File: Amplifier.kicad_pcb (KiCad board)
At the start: 2 copper layers, 140 x 54 mm, 26 parts, among them J2 Input, J3 Conn_01x04, J4 output, T1 Transformer_SP_1S, U1 6N2P, U2 6P14P

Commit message: New amplifier PCB
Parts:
- removed C1: 10uF, spdf1626_lib:C_THT_D5.0mm_P2.54mm
- removed C12, C13: 10uF, spdf1626_lib:C_THT_D10.0mm_P5.00mm
- removed J4: output, spdf1626_lib:PinHeader_1x02_P2.54mm
- removed R12: 680R, spdf1626_lib:R_THT_025W
- added C10: 10uF, spdf1626_lib:C_THT_D5.0mm_P2.5mm, F.Cu at (63.8, 55.0)
- added C4: 10uF, spdf1626_lib:C_THT_D10.0mm_P5.00mm, F.Cu at (95.9, 47.2)
- added C5: 100n, spdf1626_lib:C_THT_K73-17_P9.00mm, F.Cu at (107.1, 85.5)
- added J1: Input, spdf1626_lib:PinHeader_1x02_P2.54mm, F.Cu at (114.1, 50.7)
- added R10: 220R*, spdf1626_lib:R_THT_1W, F.Cu at (72.6, 62.0)
- C2: value 10uF -> 100n; footprint spdf1626_lib:C_THT_D5.0mm_P2.54mm -> spdf1626_lib:C_THT_K73-17_P9.00mm
- C3: value 33n opt -> 1n; footprint spdf1626_lib:C_THT_K73-17_P7.00mm -> spdf1626_lib:C_THT_K73-17_P5.00mm
- C6: value 1n -> 33n opt; footprint spdf1626_lib:C_THT_K73-17_P5.00mm -> spdf1626_lib:C_THT_K73-17_P7.00mm
- C7: value 100n -> 33n; footprint spdf1626_lib:C_THT_K73-17_P9.00mm -> spdf1626_lib:C_THT_K73-17_P7.00mm
- C8: value 33n -> 10uF; footprint spdf1626_lib:C_THT_K73-17_P7.00mm -> spdf1626_lib:C_THT_D10.0mm_P5.00mm
- C9: value 100n -> 10uF; footprint spdf1626_lib:C_THT_K73-17_P9.00mm -> spdf1626_lib:C_THT_D5.0mm_P2.5mm
- J2: value Input -> Conn_01x04; footprint spdf1626_lib:PinHeader_1x02_P2.54mm -> spdf1626_lib:PinHeader_1x04_P2.54mm
- J3: value Conn_01x04 -> output; footprint spdf1626_lib:PinHeader_1x04_P2.54mm -> spdf1626_lib:PinHeader_1x02_P2.54mm
- R1: value 6k8 -> 300k
- R2: value 220R* -> 200R; footprint spdf1626_lib:R_THT_1W -> spdf1626_lib:R_THT_025W
- R3: value 300k -> 1k8
- R4: value 1k8 -> 220k opt
- R5: value 300k -> 680R
- R6: value 200R -> 300k
- R9: value 220k opt -> 6k8
- moved J2 138.9 mm to (62.5, 49.7), turned to 90 degrees
- moved R5 106.1 mm to (84.3, 49.7), turned to 180 degrees
- moved C7 104.7 mm to (87.2, 68.6), turned to 180 degrees
- moved C9 100.0 mm to (105.1, 46.0), turned to 90 degrees
- moved R6 93.7 mm to (89.6, 85.5), turned to 0 degrees
- moved R4 90.5 mm to (89.6, 88.5), turned to 180 degrees
- moved C6 89.2 mm to (87.2, 73.8), turned to 180 degrees
- moved R8 83.6 mm to (89.6, 82.5), turned to 0 degrees
- moved RV1 81.8 mm to (89.9, 54.6), turned to 180 degrees
- moved R7 78.8 mm to (89.6, 79.5), turned to 0 degrees
- moved R9 75.2 mm to (79.9, 70.4), turned to -90 degrees
- moved U1 72.6 mm to (105.1, 68.5)
- moved C8 70.5 mm to (78.7, 92.8)
- moved U2 67.6 mm to (65.0, 80.7)
- moved R3 64.2 mm to (122.4, 83.6), turned to 90 degrees
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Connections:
- C2 pad 1: +6V -> Net-(C2-Pad1)
- C2 pad 2: GND -> Net-(C2-Pad2)
- C3 pad 2: Net-(C3-Pad2) -> GND
- C6 pad 1: Net-(C6-Pad1) -> Net-(C5-Pad2)
- C6 pad 2: GND -> Net-(C6-Pad2)
- C7 pad 2: Net-(C7-Pad2) -> Net-(C6-Pad2)
- C8 pad 1: Net-(C8-Pad1) -> 240V
- C8 pad 2: Net-(C3-Pad2) -> GND
- C9 pad 1: Net-(C9-Pad1) -> +6V
- C9 pad 2: Net-(C3-Pad1) -> GND
- J2 pad 1: Net-(C7-Pad1) -> GND
- J2 pad 2: GND -> +6V
- J3 pad 1: GND -> Left_output
- J3 pad 2: +6V -> GND
- R1 pad 1: Net-(R1-Pad1) -> Net-(C3-Pad1)
- R1 pad 2: Net-(R1-Pad2) -> Net-(C2-Pad2)
- R2 pad 1: Net-(R2-Pad1) -> Net-(C3-Pad1)
- R2 pad 2: GND -> Net-(R2-Pad2)
- R3 pad 1: Net-(C6-Pad1) -> GND
- R3 pad 2: Net-(C7-Pad2) -> Net-(C3-Pad1)
- R4 pad 1: GND -> Net-(C5-Pad2)
- R4 pad 2: Net-(C6-Pad1) -> 240V
- R5 pad 1: Net-(R5-Pad1) -> Net-(C4-Pad1)
- R5 pad 2: Net-(C9-Pad1) -> 240V
- R6 pad 1: Net-(C6-Pad1) -> Net-(R6-Pad1)
- R6 pad 2: Net-(R6-Pad2) -> Net-(C5-Pad1)
- R7 pad 1: Net-(R5-Pad1) -> Net-(R6-Pad1)
- R7 pad 2: Net-(C8-Pad1) -> Net-(C7-Pad1)
- R8 pad 1: Net-(R5-Pad1) -> Net-(R6-Pad1)
- R8 pad 2: Net-(C3-Pad1) -> Net-(C5-Pad2)
- R9 pad 1: Net-(C3-Pad1) -> Net-(R9-Pad1)
- R9 pad 2: 240V -> Net-(R9-Pad2)
- RV1 pad 1: Net-(C3-Pad2) -> GND
- RV1 pad 2: Net-(R1-Pad1) -> Net-(R9-Pad1)
- RV1 pad 3: GND -> Net-(C6-Pad2)
- U1 pad 1: Net-(C3-Pad1) -> Net-(C5-Pad2)
- U1 pad 2: Net-(C7-Pad2) -> Net-(C2-Pad2)
- U1 pad 3: Net-(R6-Pad2) -> Net-(R2-Pad2)
- U1 pad 6: Net-(C12-Pad1) -> Net-(C4-Pad1)
- U1 pad 7: Net-(C9-Pad1) -> Net-(C5-Pad1)
- U1 pad 8: Net-(C8-Pad1) -> Net-(C7-Pad1)
- U2 pad 2: Net-(R1-Pad2) -> Net-(R9-Pad2)
- U2 pad 3: Net-(R2-Pad1) -> Net-(R10-Pad1)
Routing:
- net Left_output: track 111.7 -> 7.65 mm
- net Net-(C3-Pad1): track 73.4 -> 13.4 mm
- net Net-(C5-Pad2): track 0.00 -> 45.8 mm
- net Net-(C9-Pad1): track 30.8 -> 0.00 mm
- net Net-(C5-Pad1): track 0.00 -> 30.8 mm
- net 240V: track 115.8 -> 91.6 mm
- net Net-(C8-Pad1): track 20.3 -> 0.00 mm
- net Net-(C4-Pad1): track 0.00 -> 19.1 mm
- net Net-(C12-Pad1): track 17.9 -> 0.00 mm
- net Net-(C2-Pad2): track 0.00 -> 17.1 mm
- net Net-(C6-Pad2): track 0.00 -> 16.7 mm
- net Net-(R10-Pad1): track 0.00 -> 16.2 mm
- net Net-(C7-Pad2): track 14.9 -> 0.00 mm
- net Net-(T1-Pad3): track 31.5 -> 44.5 mm
- net Net-(C6-Pad1): track 11.0 -> 0.00 mm
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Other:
- board size 140 x 54 mm -> 77 x 100 mm

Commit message: Indication board PCB
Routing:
- net Net-(C4-Pad1): track 19.1 -> 17.4 mm

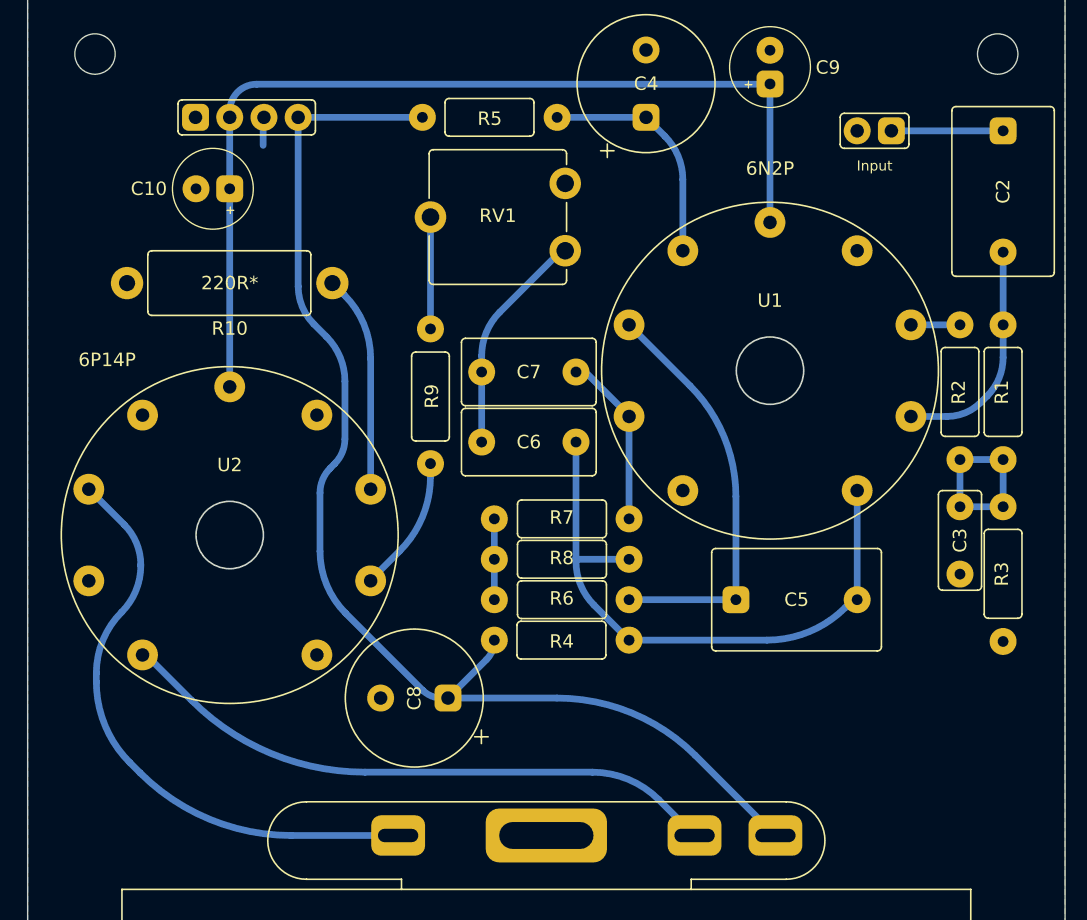
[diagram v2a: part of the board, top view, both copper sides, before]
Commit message: New 9-pin sockets
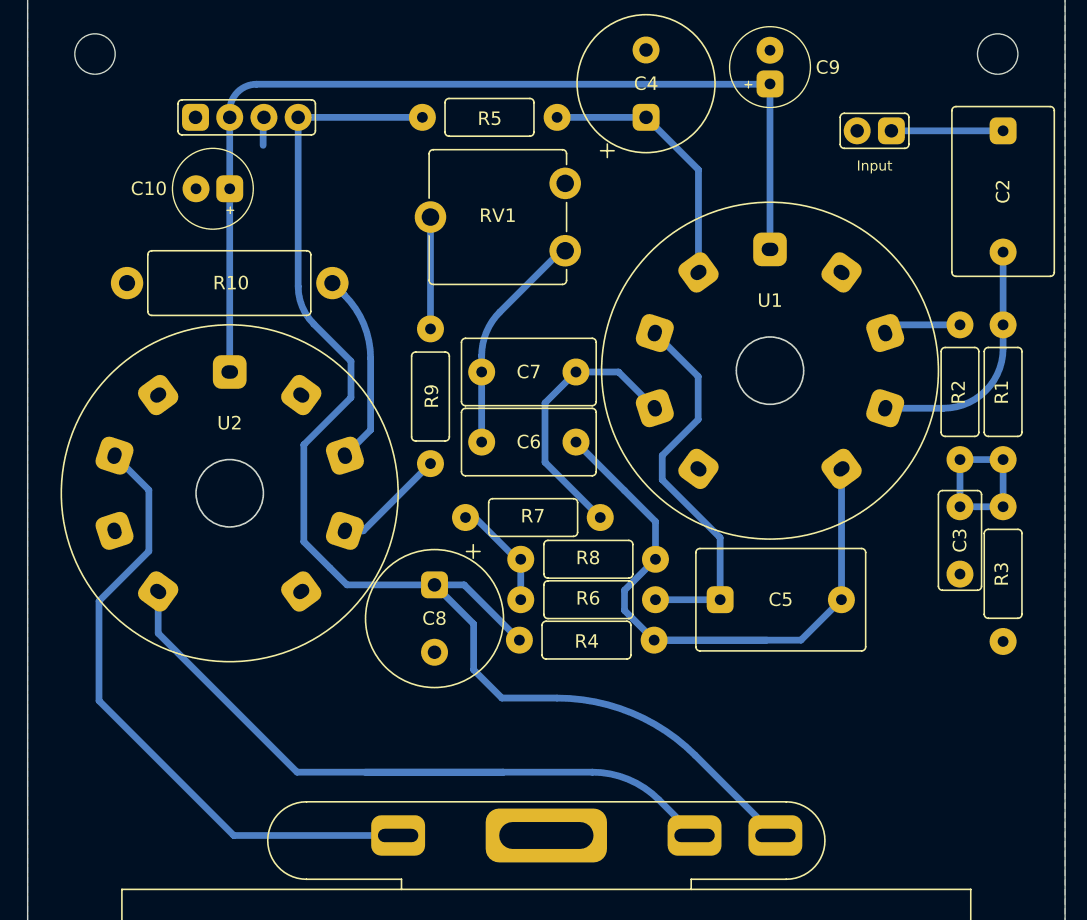
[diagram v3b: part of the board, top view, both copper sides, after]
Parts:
- U1, U2: footprint spdf1626_lib:9-pin_tube_socket -> spdf1626_lib:9-pin_tube_socket(PL9-3P)
- moved C8 6.09 mm to (80.2, 86.9), turned to -90 degrees
- moved U2 3.10 mm to (65.0, 77.6)
- moved R7 2.14 mm to (87.5, 79.4)
- moved R6 1.96 mm to (91.6, 85.5)
- moved R8 1.96 mm to (91.6, 82.5)
- moved R4 1.86 mm to (91.5, 88.5)
- moved C5 1.17 mm to (105.9, 85.5)
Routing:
- net Net-(T1-Pad2): track 45.3 -> 59.1 mm
- net Net-(C7-Pad1): track 12.0 -> 20.4 mm
- net Net-(C5-Pad2): track 45.8 -> 52.9 mm
- net 240V: track 91.6 -> 96.9 mm
- net Net-(T1-Pad3): track 44.5 -> 47.1 mm
- net Net-(R6-Pad1): track 6.00 -> 8.38 mm
- net Net-(C4-Pad1): track 17.4 -> 19.7 mm
- net Net-(R2-Pad2): track 3.64 -> 5.80 mm
- net Net-(C5-Pad1): track 30.8 -> 28.8 mm
- net Net-(R9-Pad2): track 10.2 -> 8.42 mm
- net Net-(R10-Pad1): track 16.2 -> 14.5 mm
- net Net-(C2-Pad2): track 17.1 -> 18.3 mm
- net +6V: track 71.9 -> 72.8 mm

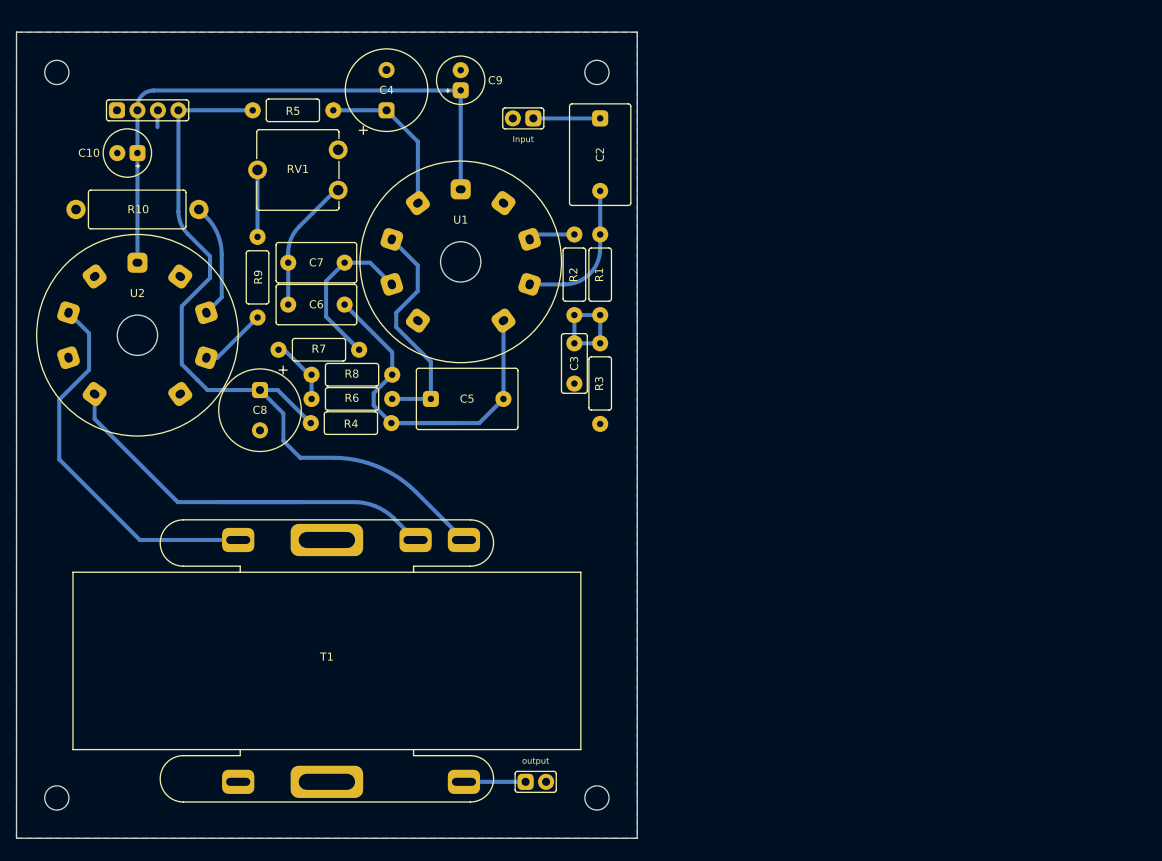
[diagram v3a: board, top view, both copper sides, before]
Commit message: New amplifier pcb
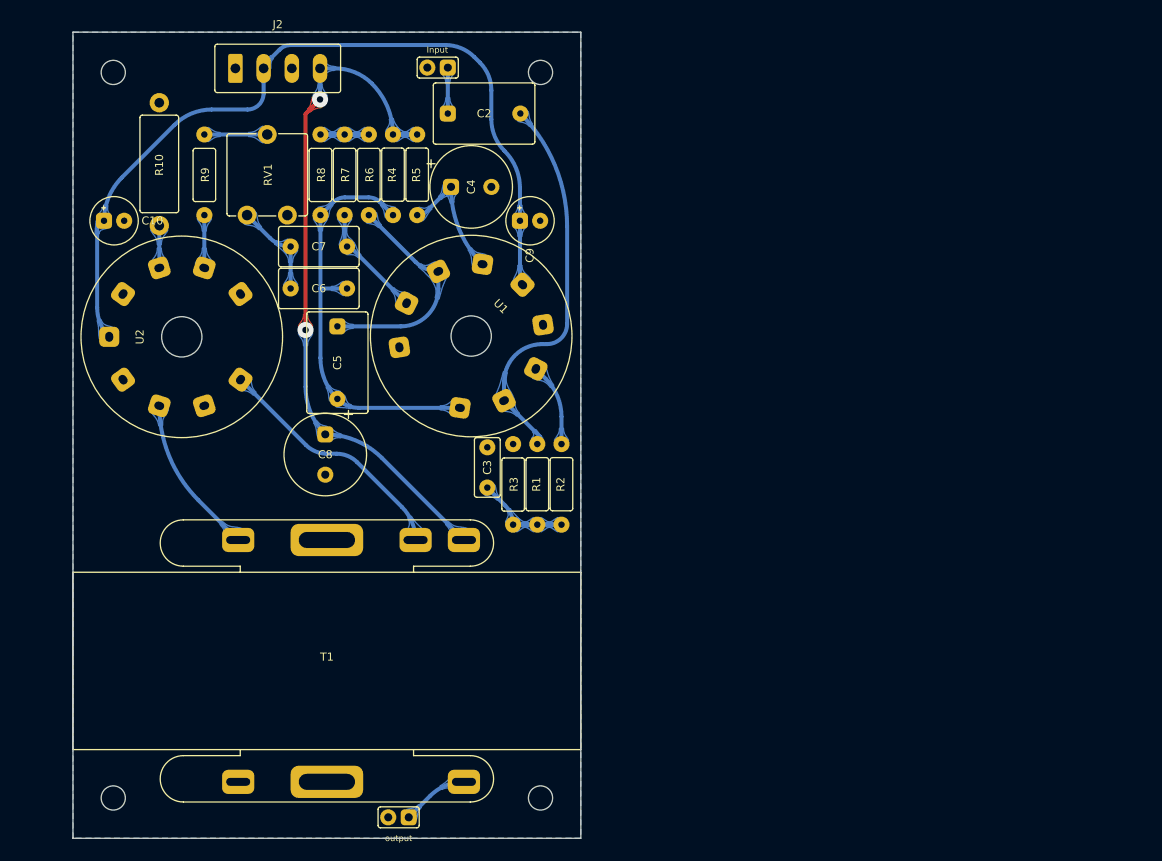
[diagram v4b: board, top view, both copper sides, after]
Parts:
- J2: footprint spdf1626_lib:PinHeader_1x04_P2.54mm -> spdf1626_lib:MCV_1,5_4-G-3.5_1x04_P3.50mm_Vertical
- moved R4 31.2 mm to (96.7, 57.7), turned to 90 degrees
- moved R6 27.9 mm to (93.7, 57.7), turned to -90 degrees
- moved R1 27.1 mm to (114.6, 96.1)
- moved R2 26.0 mm to (117.6, 96.1)
- moved R8 25.1 mm to (87.7, 57.7), turned to -90 degrees
- moved R7 21.9 mm to (90.7, 57.7), turned to -90 degrees
- moved C3 20.9 mm to (108.4, 96.5), turned to 90 degrees
- moved J2 20.6 mm to (82.4, 44.5), turned to 0 degrees
- moved C9 19.4 mm to (113.7, 63.4), turned to 0 degrees
- moved R5 17.4 mm to (99.7, 57.7), turned to 90 degrees
- moved C5 16.7 mm to (89.8, 81.0), turned to -90 degrees
- moved R3 16.5 mm to (111.6, 96.1), turned to -90 degrees
- moved C4 15.9 mm to (106.4, 59.2), turned to 0 degrees
- moved C2 15.3 mm to (108.0, 50.1), turned to 0 degrees
- moved J3 15.2 mm to (98.6, 137.4), turned to -90 degrees
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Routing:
- net +6V: track 72.8 -> 103.7 mm
- net Net-(C2-Pad2): track 18.3 -> 48.9 mm
- net Net-(T1-Pad2): track 59.1 -> 30.7 mm
- net Net-(T1-Pad3): track 47.1 -> 19.9 mm
- net 240V: track 96.9 -> 85.8 mm, vias 0 -> 2
- net Net-(R10-Pad1): track 14.5 -> 5.25 mm
- net Net-(C7-Pad1): track 20.4 -> 14.3 mm
- net Net-(C6-Pad2): track 16.7 -> 12.0 mm
- net Net-(R2-Pad2): track 5.80 -> 10.3 mm
- net Net-(C4-Pad1): track 19.7 -> 16.2 mm
- net Net-(C2-Pad1): track 8.29 -> 5.70 mm
- net Net-(R6-Pad1): track 8.38 -> 6.00 mm
- net GND: track 2.08 -> 0.00 mm
- net Net-(R9-Pad2): track 8.42 -> 6.55 mm
- net Net-(C3-Pad1): track 13.4 -> 11.8 mm
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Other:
- board size 77 x 100 mm -> 63 x 100 mm
